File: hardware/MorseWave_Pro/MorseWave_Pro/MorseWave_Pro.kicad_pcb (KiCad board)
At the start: 2 copper layers, 100 x 75 mm, 39 parts, among them J1 PADDLE_3.5mm, J2 KEY_OUT_3.5mm, J3 PTT_OUT_RCA, J4 SPEAKER_8R, J5 OLED_0.96_I2C, J6 PS2_KEYBOARD, J7 PHONES_3.5mm, Q1 BC547, U2 PC817, U3 PC817

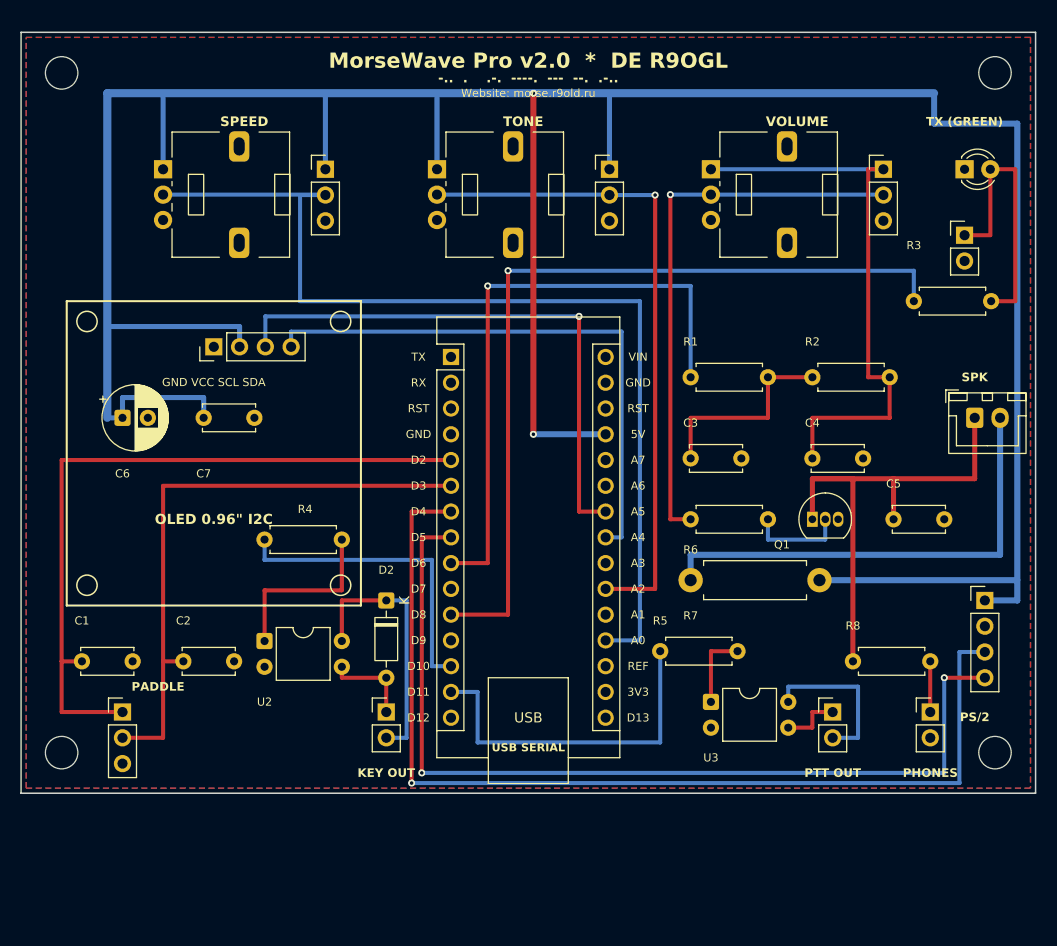
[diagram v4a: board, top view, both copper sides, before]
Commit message: feat(keyer): v2.109.12 MorseWave Pro v2.0 THT board, 3D card & breadboard starter guide
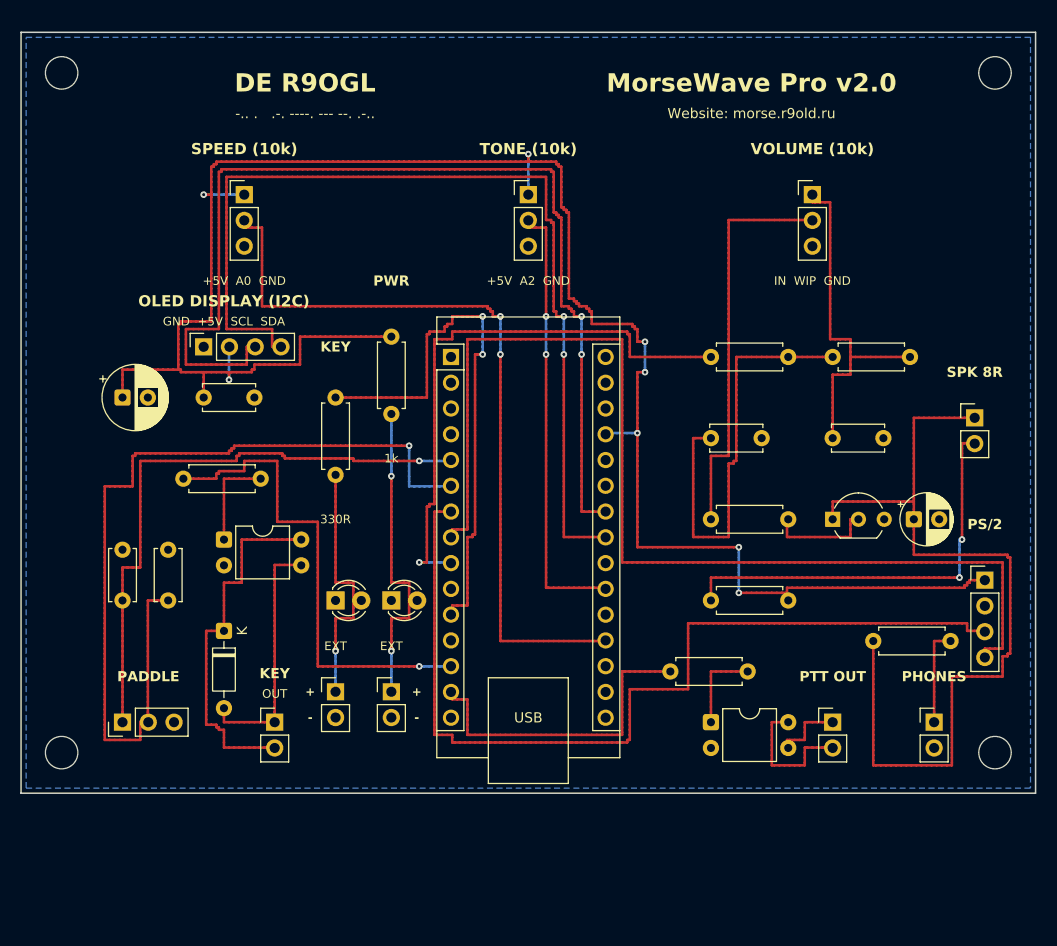
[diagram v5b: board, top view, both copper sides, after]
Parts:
- removed J_RV1: SPEED_WIRES, PinHeader_1x03_P2.54mm_Vertical
- removed J_RV2: TONE_WIRES, PinHeader_1x03_P2.54mm_Vertical
- removed J_RV3: VOL_WIRES, PinHeader_1x03_P2.54mm_Vertical
- added D3: PWR_GREEN_3mm, LED_D3.0mm, F.Cu at (36.5, 56.0)
- added J_PWR: EXT_PWR_LED, PinHeader_1x02_P2.54mm_Vertical, F.Cu at (36.5, 65.0)
- added R9: 1k, R_Axial_DIN0207_L6.3mm_D2.5mm_P7.62mm_Horizontal, F.Cu at (36.5, 30.0)
- C5: value 100nF -> 10uF; footprint C_Disc_D5.0mm_W2.5mm_P5.00mm -> CP_Radial_D5.0mm_P2.50mm
- D1: value TX_GREEN_3mm -> KEY_RED_3mm
- J4: value SPEAKER_8R -> SPK_8R; footprint JST_XH_B2B-XH-A_1x02_P2.50mm_Vertical -> PinHeader_1x02_P2.54mm_Vertical
- J5: footprint PinHeader_1x04_P2.54mm_Vertical -> PinSocket_1x04_P2.54mm_Vertical
- J_LED: value TX_LED_WIRES -> EXT_KEY_LED
- Q1: value BC547 -> 2N2222; footprint TO-92_Inline -> TO-92_Inline_Wide
- R6: value 470R -> 1k
- R7: value 33R (1W) -> 10R; footprint R_Axial_DIN0411_L9.9mm_D3.6mm_P12.70mm_Horizontal -> R_Axial_DIN0207_L6.3mm_D2.5mm_P7.62mm_Horizontal
- R8: value 150R -> 100R
- RV1: value 10k (Speed) -> SPEED (10k); footprint Potentiometer_Alps_RK09L_Single_Vertical -> PinHeader_1x03_P2.54mm_Vertical
- RV2: value 10k (Tone) -> TONE (10k); footprint Potentiometer_Alps_RK09L_Single_Vertical -> PinHeader_1x03_P2.54mm_Vertical
- RV3: value 10k (Volume) -> VOLUME (10k); footprint Potentiometer_Alps_RK09L_Single_Vertical -> PinHeader_1x03_P2.54mm_Vertical
- moved J_LED 76.6 mm to (31.0, 65.0)
- moved D1 75.2 mm to (31.0, 56.0)
- moved R3 57.8 mm to (31.0, 36.0), turned to -90 degrees
- moved D2 16.3 mm to (20.0, 59.0)
- moved J2 11.0 mm to (25.0, 68.0)
- moved U2 10.8 mm to (20.0, 50.0)
- moved RV3 10.3 mm to (78.0, 16.0)
- moved R4 10.0 mm to (16.0, 44.0)
- moved RV2 9.34 mm to (50.0, 16.0)
- moved RV1 8.38 mm to (22.0, 16.0)
- moved C1 7.21 mm to (10.0, 56.0), turned to 90 degrees
- moved C2 6.18 mm to (14.5, 56.0), turned to 90 degrees
- moved C3 2.83 mm to (68.0, 40.0)
- moved C4 2.83 mm to (80.0, 40.0)
- moved R1 2.83 mm to (68.0, 32.0)
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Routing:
- net +5V: track 293.7 -> 198.6 mm, vias 2 -> 8
- net /OLED_SCL: track 55.8 -> 103.0 mm, vias 1 -> 2
- net /OLED_SDA: track 55.9 -> 95.0 mm, vias 0 -> 2
- net Net-(J4-Pin_1): track 52.0 -> 85.2 mm
- net Net-(D3-A): track 0.00 -> 31.9 mm, vias 0 -> 2
- net /DAH: track 59.2 -> 87.5 mm, vias 0 -> 1
- net /LED_KEY: track 82.5 -> 55.2 mm, vias 1 -> 2
- net Net-(C3-Pad1): track 20.0 -> 43.2 mm
- net /POT_SPEED: track 99.3 -> 77.2 mm, vias 0 -> 2
- net Net-(C4-Pad1): track 56.7 -> 35.4 mm
- net /POT_TONE: track 65.2 -> 44.0 mm, vias 1 -> 2
- net /KEY_OUT_CTRL: track 30.9 -> 48.6 mm, vias 0 -> 1
- net /PS2_CLK: track 91.0 -> 107.0 mm, vias 2 -> 0
- net Net-(D2-A): track 8.84 -> 24.7 mm
- net Net-(R6-Pad1): track 55.0 -> 39.5 mm, vias 1 -> 0
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- removed copper zone on F.Cu, net GND
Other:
- rule pad_to_mask_clearance: 0.05 -> 0
- board text added: "+"
- board text added: "+5V A0 GND"
- board text added: "+5V A2 GND"
- board text added: "-"
- board text added: "1k"
- board text added: "330R"
- board text added: "DE R9OGL"
- board text added: "EXT"
- board text added: "GND +5V SCL SDA"
- board text added: "IN WIP GND"
- board text added: "KEY"
- board text added: "MorseWave Pro v2.0"
- board text added: "OLED DISPLAY (I2C)"
- board text added: "OUT"
- board text added: "PWR"
- board text added: "SPEED (10k)"
- board text added: "SPK 8R"
- board text added: "TONE (10k)"
- board text added: "VOLUME (10k)"
- board text removed: "3V3"
- board text removed: "5V"
- board text removed: "A0"
- board text removed: "A1"
- board text removed: "A2"
- board text removed: "A3"
- board text removed: "A4"
- board text removed: "A5"
- board text removed: "A6"
- board text removed: "A7"
- board text removed: "C1"
- board text removed: "C2"
- board text removed: "C3"
- board text removed: "C4"
- board text removed: "C5"
- board text removed: "C6"
- board text removed: "C7"
- board text removed: "D10"
- board text removed: "D11"
- board text removed: "D12"
- board text removed: "D13"
- board text removed: "D2"
- board text removed: "D3"
- board text removed: "D4"
- board text removed: "D5"
- board text removed: "D6"
- board text removed: "D7"
- board text removed: "D8"
- board text removed: "D9"
- board text removed: "GND"
- board text removed: "GND VCC SCL SDA"
- board text removed: "KEY OUT"
- board text removed: "MorseWave Pro v2.0 * DE R9OGL"
- board text removed: "OLED 0.96" I2C"
- board text removed: "Q1"
- board text removed: "R1"
- board text removed: "R2"
- board text removed: "R3"
- board text removed: "R4"
- board text removed: "R5"
- board text removed: "R6"
- board text removed: "R7"
- board text removed: "R8"
- board text removed: "REF"
- board text removed: "RST"
- board text removed: "RX"
- board text removed: "SPEED"
- board text removed: "SPK"
- board text removed: "TONE"
- board text removed: "TX"
- board text removed: "TX (GREEN)"
- board text removed: "U2"
- board text removed: "U3"
- board text removed: "USB SERIAL"
- board text removed: "VIN"
- board text removed: "VOLUME"
